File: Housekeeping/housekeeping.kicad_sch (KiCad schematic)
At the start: 0 parts

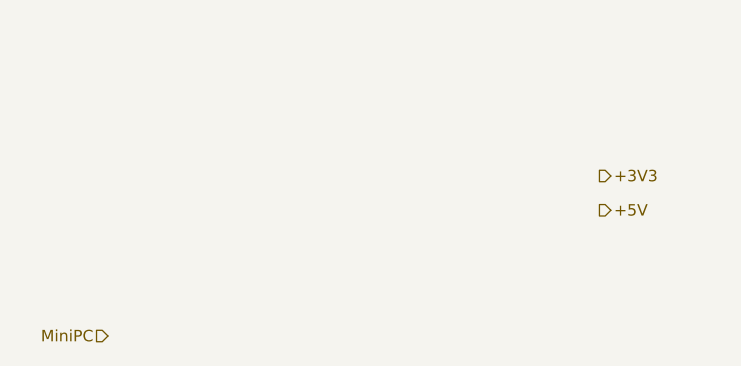
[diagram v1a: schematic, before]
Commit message: dc/dc converter
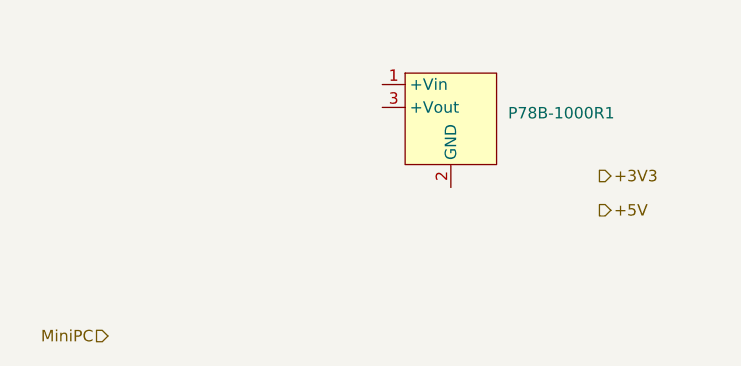
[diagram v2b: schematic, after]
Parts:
- added P78B-1000R1: ~, P78B-1000R series:P78B-1000R, symbol P78B-1000R series:P78B-1000R
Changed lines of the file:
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@@
 		)
 	)
+	(symbol
+		(lib_id "P78B-1000R series:P78B-1000R")
+		(at 133.35 86.36 0)
+		(unit 1)
+		(exclude_from_sim no)
+		(in_bom yes)
+		(on_board yes)
+		(dnp no)
+		(fields_autoplaced yes)
+		(property "Reference" "P78B-1000R1"
+			(at 139.7 85.7249 0)
+			(effects
+				(font
+					(size 1.27 1.27)
+				)
+				(justify left)
+			)
+		)
+		(property "Value" "~"
+			(at 139.7 87.63 0)
+			(effects
+				(font
+					(size 1.27 1.27)
+				)
+				(justify left)
+			)
+		)
+		(property "Footprint" "P78B-1000R series:P78B-1000R"
+			(at 133.096 95.25 0)
+			(effects
+				(font
+					(size 1.27 1.27)
+				)
+				(hide yes)
+			)
+		)
+		(property "Datasheet" ""
+			(at 133.35 86.36 0)
+			(effects
+				(font
+					(size 1.27 1.27)
+				)
+				(hide yes)
+			)
+		)
+		(property "Description" ""
+			(at 133.35 86.36 0)
+			(effects
+				(font
+					(size 1.27 1.27)
+				)
+				(hide yes)
+			)
+		)
+		(pin "1"
+		)
+		(pin "3"
+		)
+		(pin "2"
+		)
+		(instances
+			(project ""
+				(path "/54dd3bdb-fa85-45ef-ba5f-b0f6c4bf9e9e"
+					(reference "P78B-1000R1")
+					(unit 1)
+				)
+			)
+		)
+	)
+	(sheet_instances
+		(path "/"
+			(page "1")
+		)
+	)
+	(embedded_fonts no)
 )

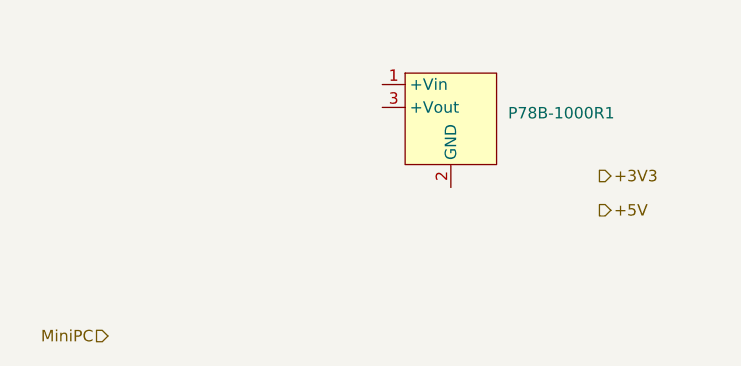
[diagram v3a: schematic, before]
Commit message: added symbol libraries and finished gate driver circuitry schematic
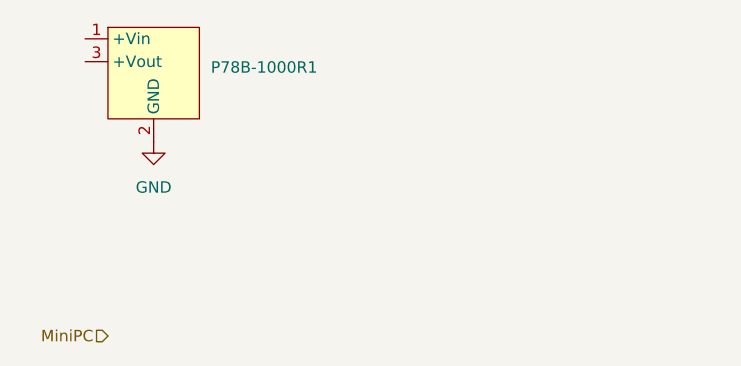
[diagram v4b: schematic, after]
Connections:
- net GND: now reaches P78B-1000R1.2 (GND)
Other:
- moved on the sheet: P78B-1000R1
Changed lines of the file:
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@@
 	(generator_version "9.0")
 	(paper "A4")
-	(hierarchical_label "+5V"
-		(shape output)
-		(at 149.86 96.52 0)
-		(effects
-			(font
-				(size 1.27 1.27)
-			)
-			(justify left)
-		)
-	)
 	(hierarchical_label "MiniPC"
 		(shape input)
@@
 		)
 	)
-	(hierarchical_label "+3V3"
-		(shape output)
-		(at 149.86 92.71 0)
-		(effects
-			(font
-				(size 1.27 1.27)
+	(symbol
+		(lib_id "power:GND")
+		(at 100.33 88.9 0)
+		(unit 1)
+		(exclude_from_sim no)
+		(in_bom yes)
+		(on_board yes)
+		(dnp no)
+		(fields_autoplaced yes)
+		(property "Reference" "#PWR07"
+			(at 100.33 95.25 0)
+			(effects
+				(font
+					(size 1.27 1.27)
+				)
+				(hide yes)
 			)
-			(justify left)
+		)
+		(property "Value" "GND"
+			(at 100.33 93.98 0)
+			(effects
+				(font
+					(size 1.27 1.27)
+				)
+			)
+		)
+		(property "Footprint" ""
+			(at 100.33 88.9 0)
+			(effects
+				(font
+					(size 1.27 1.27)
+				)
+				(hide yes)
+			)
+		)
+		(property "Datasheet" ""
+			(at 100.33 88.9 0)
+			(effects
+				(font
+					(size 1.27 1.27)
+				)
+				(hide yes)
+			)
+		)
+		(property "Description" "Power symbol creates a global label with name \"GND\" , ground"
+			(at 100.33 88.9 0)
+			(effects
+				(font
+					(size 1.27 1.27)
+				)
+				(hide yes)
+			)
+		)
+		(pin "1"
+		)
+		(instances
+			(project "Supercap"
+				(path "/98ee8313-37ab-4329-91ab-b5710476f82f/47f13d7b-df0e-4361-81b8-c133778882c5"
+					(reference "#PWR07")
+					(unit 1)
+				)
+			)
 		)
 	)
 	(symbol
 		(lib_id "P78B-1000R series:P78B-1000R")
-		(at 133.35 86.36 0)
+		(at 100.33 81.28 0)
 		(unit 1)
 		(exclude_from_sim no)
@@
 		(fields_autoplaced yes)
 		(property "Reference" "P78B-1000R?"
-			(at 139.7 85.7249 0)
+			(at 106.68 80.6449 0)
 			(effects
 				(font
@@
 		)
 		(property "Value" "~"
-			(at 139.7 87.63 0)
+			(at 106.68 82.55 0)
 			(effects
 				(font
@@
 		)
 		(property "Footprint" "P78B-1000R series:P78B-1000R"
-			(at 133.096 95.25 0)
+			(at 100.076 90.17 0)
 			(effects
 				(font
@@
 			)
 		)
-		(property "Datasheet" ""
-			(at 133.35 86.36 0)
+		(property "Datasheet" "https://www.belfuse.com/media/datasheets/products/power-supplies/P78B-1000.pdf"
+			(at 100.33 81.28 0)
 			(effects
 				(font
@@
 		)
 		(property "Description" ""
-			(at 133.35 86.36 0)
+			(at 100.33 81.28 0)
 			(effects
 				(font

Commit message: housekeeping_2
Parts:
- added P7809B-1000R: ~, P78B-1000R series:P78B-1000R, symbol P78B-1000R series:P78B-1000R
- renumbered P78B-1000R1 to P7803B-1000R
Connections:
- net GND: now also P7809B-1000R.2 (GND)
- net 24: now reaches P7803B-1000R.1 (+Vin)
- net 3.3V: now reaches P7803B-1000R.3 (+Vout)
- new net 24V: P7809B-1000R.1 (+Vin)
- new net 9V: P7809B-1000R.3 (+Vout)
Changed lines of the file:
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@@
 	(generator_version "9.0")
 	(paper "A4")
-	(hierarchical_label "MiniPC"
+	(hierarchical_label "24"
 		(shape input)
-		(at 95.25 110.49 180)
+		(at 92.71 77.47 180)
 		(effects
 			(font
@@
 			)
 			(justify right)
+		)
+	)
+	(hierarchical_label "3.3V"
+		(shape input)
+		(at 92.71 80.01 180)
+		(effects
+			(font
+				(size 1.27 1.27)
+			)
+			(justify right)
+		)
+	)
+	(hierarchical_label "24V"
+		(shape input)
+		(at 133.35 77.47 180)
+		(effects
+			(font
+				(size 1.27 1.27)
+			)
+			(justify right)
+		)
+	)
+	(hierarchical_label "9V"
+		(shape input)
+		(at 133.35 80.01 180)
+		(effects
+			(font
+				(size 1.27 1.27)
+			)
+			(justify right)
+		)
+	)
+	(symbol
+		(lib_id "power:GND")
+		(at 140.97 88.9 0)
+		(unit 1)
+		(exclude_from_sim no)
+		(in_bom yes)
+		(on_board yes)
+		(dnp no)
+		(fields_autoplaced yes)
+		(property "Reference" "#PWR011"
+			(at 140.97 95.25 0)
+			(effects
+				(font
+					(size 1.27 1.27)
+				)
+				(hide yes)
+			)
+		)
+		(property "Value" "GND"
+			(at 140.97 93.98 0)
+			(effects
+				(font
+					(size 1.27 1.27)
+				)
+			)
+		)
+		(property "Footprint" ""
+			(at 140.97 88.9 0)
+			(effects
+				(font
+					(size 1.27 1.27)
+				)
+				(hide yes)
+			)
+		)
+		(property "Datasheet" ""
+			(at 140.97 88.9 0)
+			(effects
+				(font
+					(size 1.27 1.27)
+				)
+				(hide yes)
+			)
+		)
+		(property "Description" "Power symbol creates a global label with name \"GND\" , ground"
+			(at 140.97 88.9 0)
+			(effects
+				(font
+					(size 1.27 1.27)
+				)
+				(hide yes)
+			)
+		)
+		(pin "1"
+		)
+		(instances
+			(project ""
+				(path "/98ee8313-37ab-4329-91ab-b5710476f82f/47f13d7b-df0e-4361-81b8-c133778882c5"
+					(reference "#PWR011")
+					(unit 1)
+				)
+			)
 		)
 	)
@@
 	(symbol
 		(lib_id "P78B-1000R series:P78B-1000R")
+		(at 140.97 81.28 0)
+		(unit 1)
+		(exclude_from_sim no)
+		(in_bom yes)
+		(on_board yes)
+		(dnp no)
+		(fields_autoplaced yes)
+		(property "Reference" "P7809B-1000R"
+			(at 147.32 80.6449 0)
+			(effects
+				(font
+					(size 1.27 1.27)
+				)
+				(justify left)
+			)
+		)
+		(property "Value" "~"
+			(at 147.32 82.55 0)
+			(effects
+				(font
+					(size 1.27 1.27)
+				)
+				(justify left)
+			)
+		)
+		(property "Footprint" "P78B-1000R series:P78B-1000R"
+			(at 140.716 90.17 0)
+			(effects
+				(font
+					(size 1.27 1.27)
+				)
+				(hide yes)
+			)
+		)
+		(property "Datasheet" "https://www.belfuse.com/media/datasheets/products/power-supplies/P78B-1000.pdf"
+			(at 140.97 81.28 0)
+			(effects
+				(font
+					(size 1.27 1.27)
+				)
+				(hide yes)
+			)
+		)
+		(property "Description" ""
+			(at 140.97 81.28 0)
+			(effects
+				(font
+					(size 1.27 1.27)
+				)
+				(hide yes)
+			)
+		)
+		(pin "1"
+		)
+		(pin "3"
+		)
+		(pin "2"
+		)
+		(instances
+			(project "Supercap"
+				(path "/98ee8313-37ab-4329-91ab-b5710476f82f/47f13d7b-df0e-4361-81b8-c133778882c5"
+					(reference "P7809B-1000R")
+					(unit 1)
+				)
+			)
+		)
+	)
+	(symbol
+		(lib_id "P78B-1000R series:P78B-1000R")
 		(at 100.33 81.28 0)
 		(unit 1)
@@
 		(dnp no)
 		(fields_autoplaced yes)
-		(property "Reference" "P78B-1000R?"
+		(property "Reference" "P7803B-1000R"
 			(at 106.68 80.6449 0)
 			(effects
@@
 			(project "Supercap"
 				(path "/98ee8313-37ab-4329-91ab-b5710476f82f/47f13d7b-df0e-4361-81b8-c133778882c5"
-					(reference "P78B-1000R?")
-					(unit 1)
-				)
+					(reference "P7803B-1000R")
+					(unit 1)
+				)
